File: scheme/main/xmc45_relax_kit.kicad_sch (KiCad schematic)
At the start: 1 part

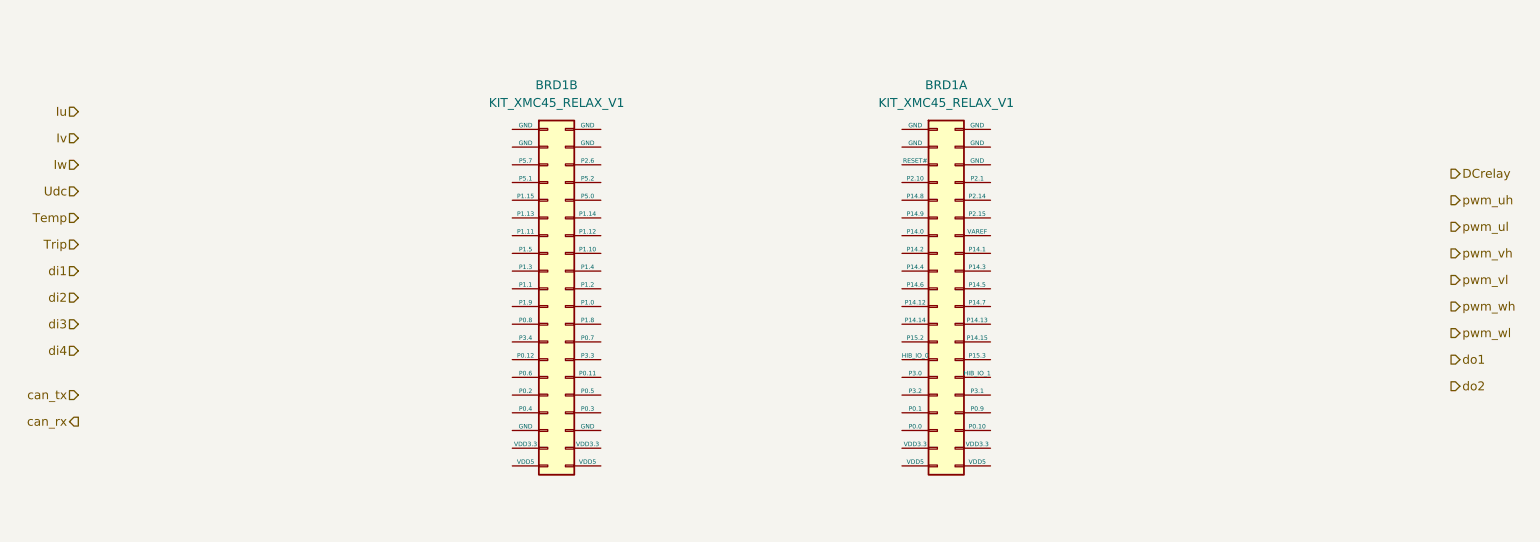
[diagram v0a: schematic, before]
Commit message: xmc45 relax kit connections
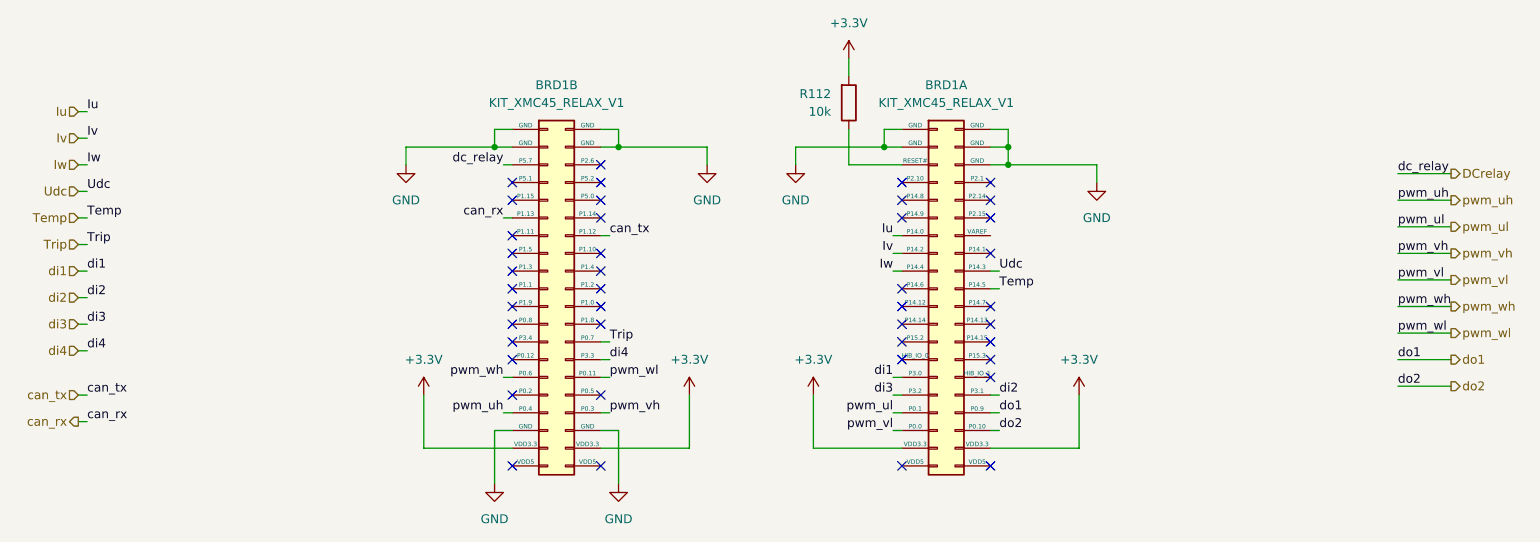
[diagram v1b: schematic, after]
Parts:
- added R112: 10k, Resistor_SMD:R_0805_2012Metric, symbol Device:R
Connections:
- net DCrelay: now also BRD1.6 (P5.7)
- net Iu: now also BRD1.14 (P14.0)
- net Iv: now also BRD1.16 (P14.2)
- net Iw: now also BRD1.18 (P14.4)
- net Temp: now also BRD1.19 (P14.5)
- net Trip: now also BRD1.25 (P0.7)
- net Udc: now also BRD1.17 (P14.3)
- net can_rx: now also BRD1.12 (P1.13)
- net can_tx: now also BRD1.13 (P1.12)
- net di1: now also BRD1.30 (P3.0)
- net di2: now also BRD1.31 (P3.1)
- net di3: now also BRD1.32 (P3.2)
- net di4: now also BRD1.27 (P3.3)
- net do1: now also BRD1.33 (P0.9)
- net do2: now also BRD1.35 (P0.10)
- net pwm_uh: now also BRD1.34 (P0.4)
- net pwm_ul: now also BRD1.34 (P0.1)
- net pwm_vh: now also BRD1.33 (P0.3)
- net pwm_vl: now also BRD1.36 (P0.0)
- net pwm_wh: now also BRD1.30 (P0.6)
- net pwm_wl: now also BRD1.29 (P0.11)
- net GND: now reaches BRD1.1 (GND)
- net GND: now also BRD1.1 (GND), BRD1.2 (GND), BRD1.2 (GND), BRD1.3 (GND), BRD1.3 (GND), BRD1.35 (GND), BRD1.36 (GND), BRD1.4 (GND), BRD1.4 (GND), BRD1.5 (GND)
- net +3.3V: now reaches BRD1.37 (VDD3.3)
- net +3.3V: now also BRD1.37 (VDD3.3), BRD1.38 (VDD3.3), BRD1.38 (VDD3.3), R112.2
- net at BRD1.6 (RESET#): now also R112.1
- no-connect marks 0 -> 42

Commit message: added adc driver & output buffer with oe
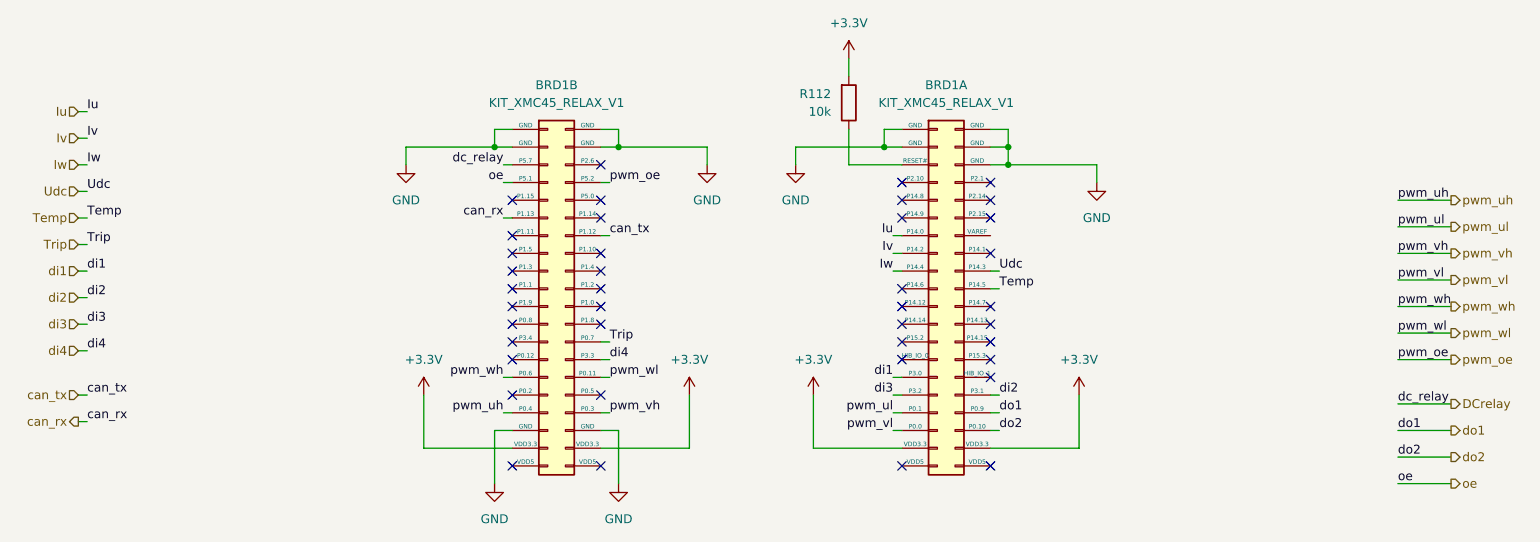
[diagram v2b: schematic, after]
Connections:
- net pwm_oe: now reaches BRD1.7 (P5.2)
- net oe: now reaches BRD1.8 (P5.1)
- no-connect marks 42 -> 40

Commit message: added xmc45 relax kit footprint
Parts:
- BRD1: footprint (none) -> main:XMC45_RELAX_KIT_V1
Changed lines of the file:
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@@
 			)
 		)
-		(property "Footprint" ""
+		(property "Footprint" "main:XMC45_RELAX_KIT_V1"
 			(at 110.49 78.74 0)
 			(effects
@@
 			)
 		)
-		(property "Footprint" ""
+		(property "Footprint" "main:XMC45_RELAX_KIT_V1"
 			(at 166.37 78.74 0)
 			(effects

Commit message: control boards symbols & footprints updated
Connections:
- net +3.3V: now also BRD1.X1_37 (VDD3.3), BRD1.X1_38 (VDD3.3), BRD1.X2_37 (VDD3.3), BRD1.X2_38 (VDD3.3); no longer BRD1.37 (VDD3.3), BRD1.37 (VDD3.3), BRD1.38 (VDD3.3), BRD1.38 (VDD3.3)
- net DCrelay: now also BRD1.X2_6 (P5.7); no longer BRD1.6 (P5.7)
- net GND: now also BRD1.X1_1 (GND), BRD1.X1_2 (GND), BRD1.X1_3 (GND), BRD1.X1_4 (GND), BRD1.X1_5 (GND), BRD1.X2_1 (GND), BRD1.X2_2 (GND), BRD1.X2_3 (GND), BRD1.X2_35 (GND), BRD1.X2_36 (GND), BRD1.X2_4 (GND); no longer BRD1.1 (GND), BRD1.1 (GND), BRD1.2 (GND), BRD1.2 (GND), BRD1.3 (GND), BRD1.3 (GND), BRD1.35 (GND), BRD1.36 (GND), BRD1.4 (GND), BRD1.4 (GND), BRD1.5 (GND)
- net Iu: now also BRD1.X1_14 (P14.0); no longer BRD1.14 (P14.0)
- net Iv: now also BRD1.X1_16 (P14.2); no longer BRD1.16 (P14.2)
- net Iw: now also BRD1.X1_18 (P14.4); no longer BRD1.18 (P14.4)
- net Temp: now also BRD1.X1_19 (P14.5); no longer BRD1.19 (P14.5)
- net Trip: now also BRD1.X2_25 (P0.7); no longer BRD1.25 (P0.7)
- net Udc: now also BRD1.X1_17 (P14.3); no longer BRD1.17 (P14.3)
- net can_rx: now also BRD1.X2_12 (P1.13); no longer BRD1.12 (P1.13)
- net can_tx: now also BRD1.X2_13 (P1.12); no longer BRD1.13 (P1.12)
- net di1: now also BRD1.X1_30 (P3.0); no longer BRD1.30 (P3.0)
- net di2: now also BRD1.X1_31 (P3.1); no longer BRD1.31 (P3.1)
- net di3: now also BRD1.X1_32 (P3.2); no longer BRD1.32 (P3.2)
- net di4: now also BRD1.X2_27 (P3.3); no longer BRD1.27 (P3.3)
- net do1: now also BRD1.X1_33 (P0.9); no longer BRD1.33 (P0.9)
- net do2: now also BRD1.X1_35 (P0.10); no longer BRD1.35 (P0.10)
- net oe: now also BRD1.X2_8 (P5.1); no longer BRD1.8 (P5.1)
- net pwm_oe: now also BRD1.X2_7 (P5.2); no longer BRD1.7 (P5.2)
- net pwm_uh: now also BRD1.X2_34 (P0.4); no longer BRD1.34 (P0.4)
- net pwm_ul: now also BRD1.X1_34 (P0.1); no longer BRD1.34 (P0.1)
- net pwm_vh: now also BRD1.X2_33 (P0.3); no longer BRD1.33 (P0.3)
- net pwm_vl: now also BRD1.X1_36 (P0.0); no longer BRD1.36 (P0.0)
- net pwm_wh: now also BRD1.X2_30 (P0.6); no longer BRD1.30 (P0.6)
- net pwm_wl: now also BRD1.X2_29 (P0.11); no longer BRD1.29 (P0.11)
- net at R112.1: now also BRD1.X1_6 (RESET#); no longer BRD1.6 (RESET#)

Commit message: sheets titles
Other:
- title: (none) -> Плата KIT_XMC45_RELAX_V1
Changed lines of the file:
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@@
 	(generator_version "8.0")
 	(paper "A4")
+	(title_block
+		(title "Плата KIT_XMC45_RELAX_V1")
+	)
 	(junction
 		(at 119.38 58.42)

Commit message: fixed check errors
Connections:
- net +3.3VA: now reaches BRD1.X1_13 (VAREF)
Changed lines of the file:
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@@
+	(wire
+		(pts
+			(xy 179.07 68.58) (xy 179.07 71.12)
+		)
+		(stroke
+			(width 0)
+			(type default)
+		)
+	)
 	(wire
 		(pts
@@
 		(pts
 			(xy 102.87 60.96) (xy 104.14 60.96)
+		)
+		(stroke
+			(width 0)
+			(type default)
+		)
+	)
+	(wire
+		(pts
+			(xy 179.07 71.12) (xy 172.72 71.12)
 		)
 		(stroke
@@
 		(dnp no)
 		(fields_autoplaced yes)
-		(property "Reference" "#PWR117"
+		(property "Reference" "#PWR0117"
 			(at 88.9 67.31 0)
 			(effects
@@
 			(project "main"
 				(path "/c11d1dbc-4db9-4712-8d1d-5f6f7086cded/e3db07b5-d47c-4d55-bf51-a423335924fb/6525718b-1ee0-4b4a-b427-5961f80d0d97"
-					(reference "#PWR117")
+					(reference "#PWR0117")
 					(unit 1)
 				)
@@
 		(dnp no)
 		(fields_autoplaced yes)
-		(property "Reference" "#PWR123"
+		(property "Reference" "#PWR0123"
 			(at 152.4 49.53 0)
 			(effects
@@
 			(project "main"
 				(path "/c11d1dbc-4db9-4712-8d1d-5f6f7086cded/e3db07b5-d47c-4d55-bf51-a423335924fb/6525718b-1ee0-4b4a-b427-5961f80d0d97"
-					(reference "#PWR123")
+					(reference "#PWR0123")
+					(unit 1)
+				)
+			)
+		)
+	)
+	(symbol
+		(lib_id "power:+3.3VA")
+		(at 179.07 68.58 0)
+		(unit 1)
+		(exclude_from_sim no)
+		(in_bom yes)
+		(on_board yes)
+		(dnp no)
+		(fields_autoplaced yes)
+		(property "Reference" "#PWR015"
+			(at 179.07 72.39 0)
+			(effects
+				(font
+					(size 1.27 1.27)
+				)
+				(hide yes)
+			)
+		)
+		(property "Value" "+3.3VA"
+			(at 179.07 63.5 0)
+			(effects
+				(font
+					(size 1.27 1.27)
+				)
+			)
+		)
+		(property "Footprint" ""
+			(at 179.07 68.58 0)
+			(effects
+				(font
+					(size 1.27 1.27)
+				)
+				(hide yes)
+			)
+		)
+		(property "Datasheet" ""
+			(at 179.07 68.58 0)
+			(effects
+				(font
+					(size 1.27 1.27)
+				)
+				(hide yes)
+			)
+		)
+		(property "Description" "Power symbol creates a global label with name \"+3.3VA\""
+			(at 179.07 68.58 0)
+			(effects
+				(font
+					(size 1.27 1.27)
+				)
+				(hide yes)
+			)
+		)
+		(pin "1"
+		)
+		(instances
+			(project ""
+				(path "/c11d1dbc-4db9-4712-8d1d-5f6f7086cded/e3db07b5-d47c-4d55-bf51-a423335924fb/6525718b-1ee0-4b4a-b427-5961f80d0d97"
+					(reference "#PWR015")
 					(unit 1)
 				)
@@
 		(dnp no)
 		(fields_autoplaced yes)
-		(property "Reference" "#PWR122"
+		(property "Reference" "#PWR0122"
 			(at 101.6 113.03 0)
 			(effects
@@
 			(project "main"
 				(path "/c11d1dbc-4db9-4712-8d1d-5f6f7086cded/e3db07b5-d47c-4d55-bf51-a423335924fb/6525718b-1ee0-4b4a-b427-5961f80d0d97"
-					(reference "#PWR122")
+					(reference "#PWR0122")
 					(unit 1)
 				)
@@
 		(dnp no)
 		(fields_autoplaced yes)
-		(property "Reference" "#PWR120"
+		(property "Reference" "#PWR0120"
 			(at 144.78 67.31 0)
 			(effects
@@
 			(project "main"
 				(path "/c11d1dbc-4db9-4712-8d1d-5f6f7086cded/e3db07b5-d47c-4d55-bf51-a423335924fb/6525718b-1ee0-4b4a-b427-5961f80d0d97"
-					(reference "#PWR120")
+					(reference "#PWR0120")
 					(unit 1)
 				)
@@
 		(dnp no)
 		(fields_autoplaced yes)
-		(property "Reference" "#PWR127"
+		(property "Reference" "#PWR0127"
 			(at 147.32 97.79 0)
 			(effects
@@
 			(project "main"
 				(path "/c11d1dbc-4db9-4712-8d1d-5f6f7086cded/e3db07b5-d47c-4d55-bf51-a423335924fb/6525718b-1ee0-4b4a-b427-5961f80d0d97"
-					(reference "#PWR127")
+					(reference "#PWR0127")
 					(unit 1)
 				)
@@
 		(dnp no)
 		(fields_autoplaced yes)
-		(property "Reference" "#PWR118"
+		(property "Reference" "#PWR0118"
 			(at 132.08 67.31 0)
 			(effects
@@
 			(project "main"
 				(path "/c11d1dbc-4db9-4712-8d1d-5f6f7086cded/e3db07b5-d47c-4d55-bf51-a423335924fb/6525718b-1ee0-4b4a-b427-5961f80d0d97"
-					(reference "#PWR118")
+					(reference "#PWR0118")
 					(unit 1)
 				)
@@
 		(dnp no)
 		(fields_autoplaced yes)
-		(property "Reference" "#PWR119"
+		(property "Reference" "#PWR0119"
 			(at 187.96 69.85 0)
 			(effects
@@
 			(project "main"
 				(path "/c11d1dbc-4db9-4712-8d1d-5f6f7086cded/e3db07b5-d47c-4d55-bf51-a423335924fb/6525718b-1ee0-4b4a-b427-5961f80d0d97"
-					(reference "#PWR119")
+					(reference "#PWR0119")
 					(unit 1)
 				)
@@
 		(dnp no)
 		(fields_autoplaced yes)
-		(property "Reference" "#PWR125"
+		(property "Reference" "#PWR0125"
 			(at 129.54 97.79 0)
 			(effects
@@
 			(project "main"
 				(path "/c11d1dbc-4db9-4712-8d1d-5f6f7086cded/e3db07b5-d47c-4d55-bf51-a423335924fb/6525718b-1ee0-4b4a-b427-5961f80d0d97"
-					(reference "#PWR125")
+					(reference "#PWR0125")
 					(unit 1)
 				)
@@
 		(dnp no)
 		(fields_autoplaced yes)
-		(property "Reference" "#PWR121"
+		(property "Reference" "#PWR0121"
 			(at 119.38 113.03 0)
 			(effects
@@
 			(project "main"
 				(path "/c11d1dbc-4db9-4712-8d1d-5f6f7086cded/e3db07b5-d47c-4d55-bf51-a423335924fb/6525718b-1ee0-4b4a-b427-5961f80d0d97"
-					(reference "#PWR121")
+					(reference "#PWR0121")
 					(unit 1)
 				)
@@
 		(dnp no)
 		(fields_autoplaced yes)
-		(property "Reference" "#PWR124"
+		(property "Reference" "#PWR0124"
 			(at 91.44 97.79 0)
 			(effects
@@
 			(project "main"
 				(path "/c11d1dbc-4db9-4712-8d1d-5f6f7086cded/e3db07b5-d47c-4d55-bf51-a423335924fb/6525718b-1ee0-4b4a-b427-5961f80d0d97"
-					(reference "#PWR124")
+					(reference "#PWR0124")
 					(unit 1)
 				)
@@
 		(dnp no)
 		(fields_autoplaced yes)
-		(property "Reference" "#PWR126"
+		(property "Reference" "#PWR0126"
 			(at 185.42 97.79 0)
 			(effects
@@
 			(project "main"
 				(path "/c11d1dbc-4db9-4712-8d1d-5f6f7086cded/e3db07b5-d47c-4d55-bf51-a423335924fb/6525718b-1ee0-4b4a-b427-5961f80d0d97"
-					(reference "#PWR126")
+					(reference "#PWR0126")
 					(unit 1)
 				)

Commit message: added analog input 0 && sheets sort
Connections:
- net Temp: now also BRD1.X1_17 (P14.3); no longer BRD1.X1_19 (P14.5)
- net Udc: now also BRD1.X1_15 (P14.1); no longer BRD1.X1_17 (P14.3)
- new net ain0: BRD1.X1_19 (P14.5)
- no-connect marks 40 -> 39
